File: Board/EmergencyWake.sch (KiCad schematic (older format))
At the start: 128 parts, among them J1 USB_C_Receptacle_USB2.0, J2 Micro_SD_Card_Det, J3 Conn_01x03, J4 Conn_01x02, J5 Conn_01x03, J6 Conn_01x04, J7 Conn_01x02, J8 Conn_01x04, J9 Conn_01x04, Q1 AO3400A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

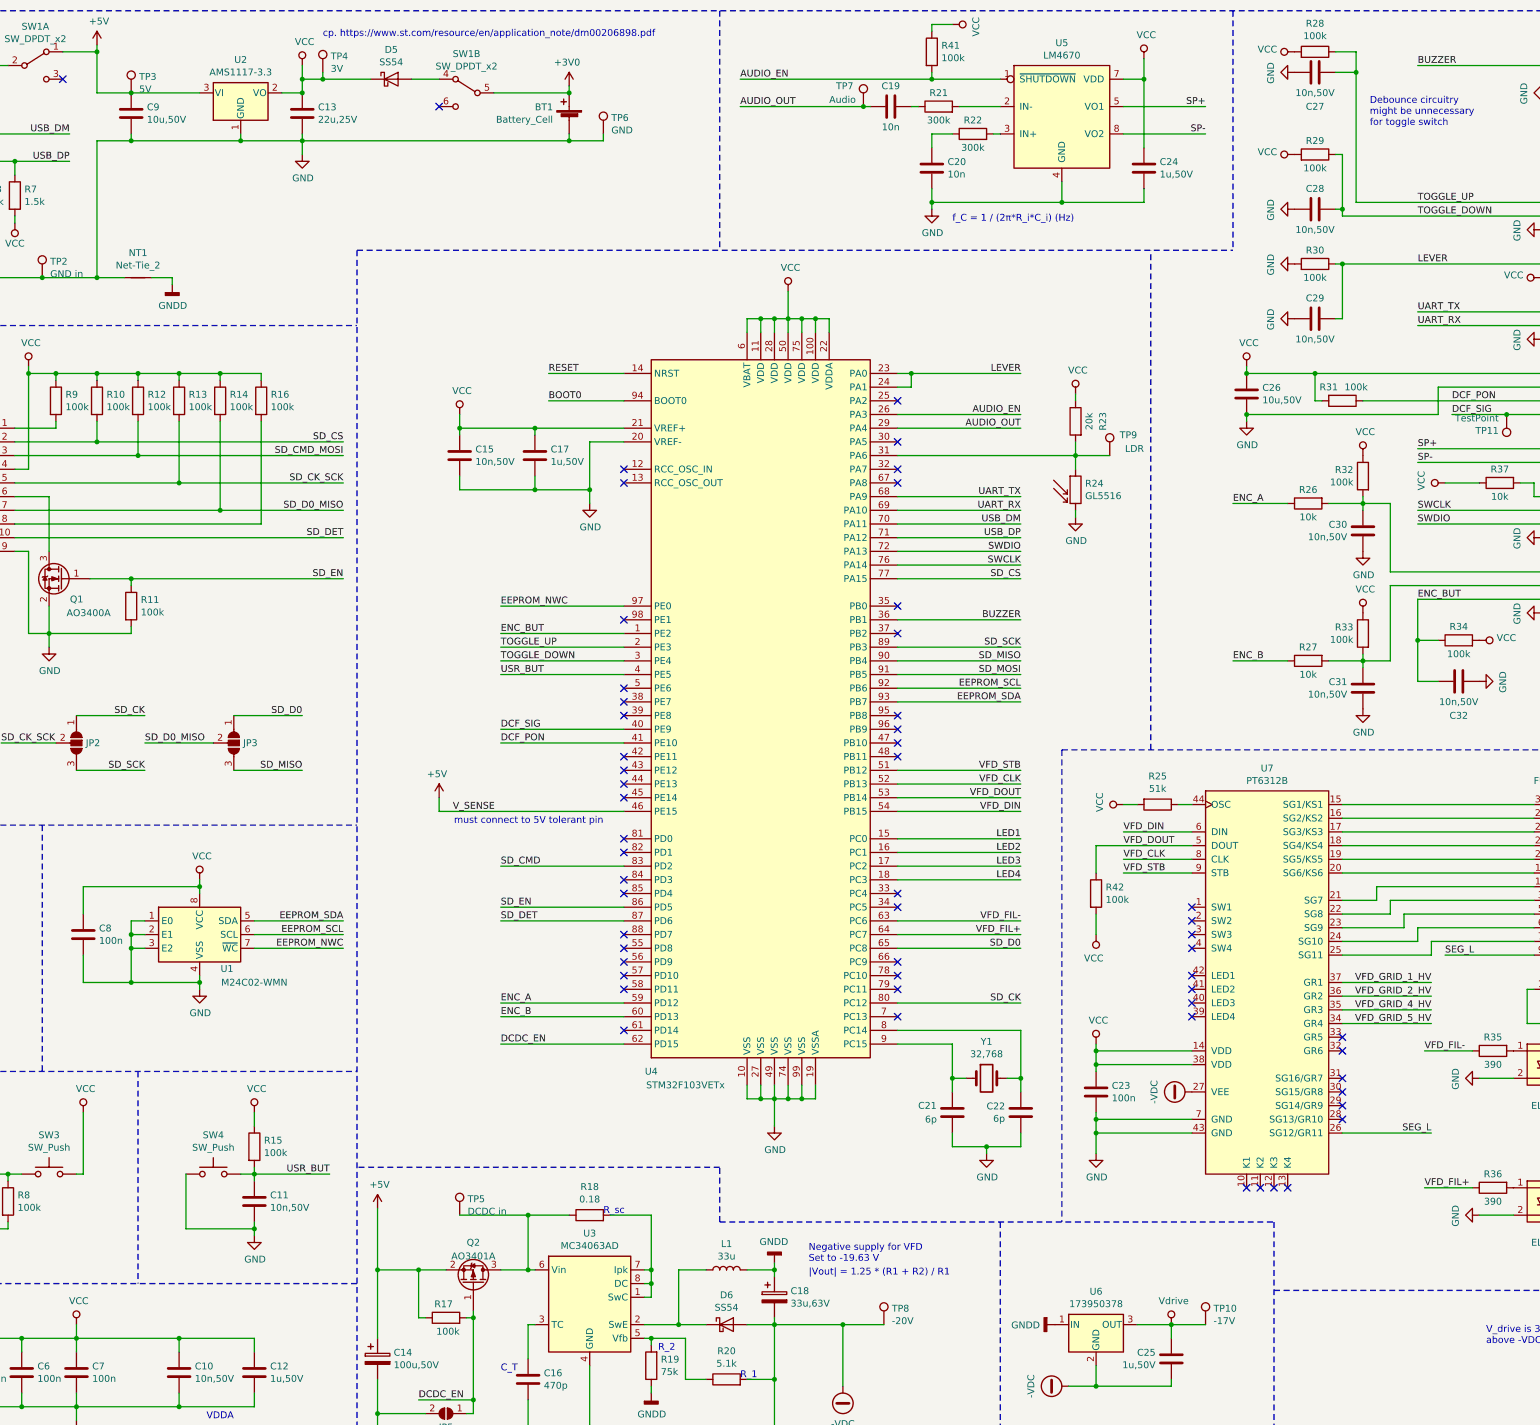
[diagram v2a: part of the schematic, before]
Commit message: [Board] Cleaned up silkscreen
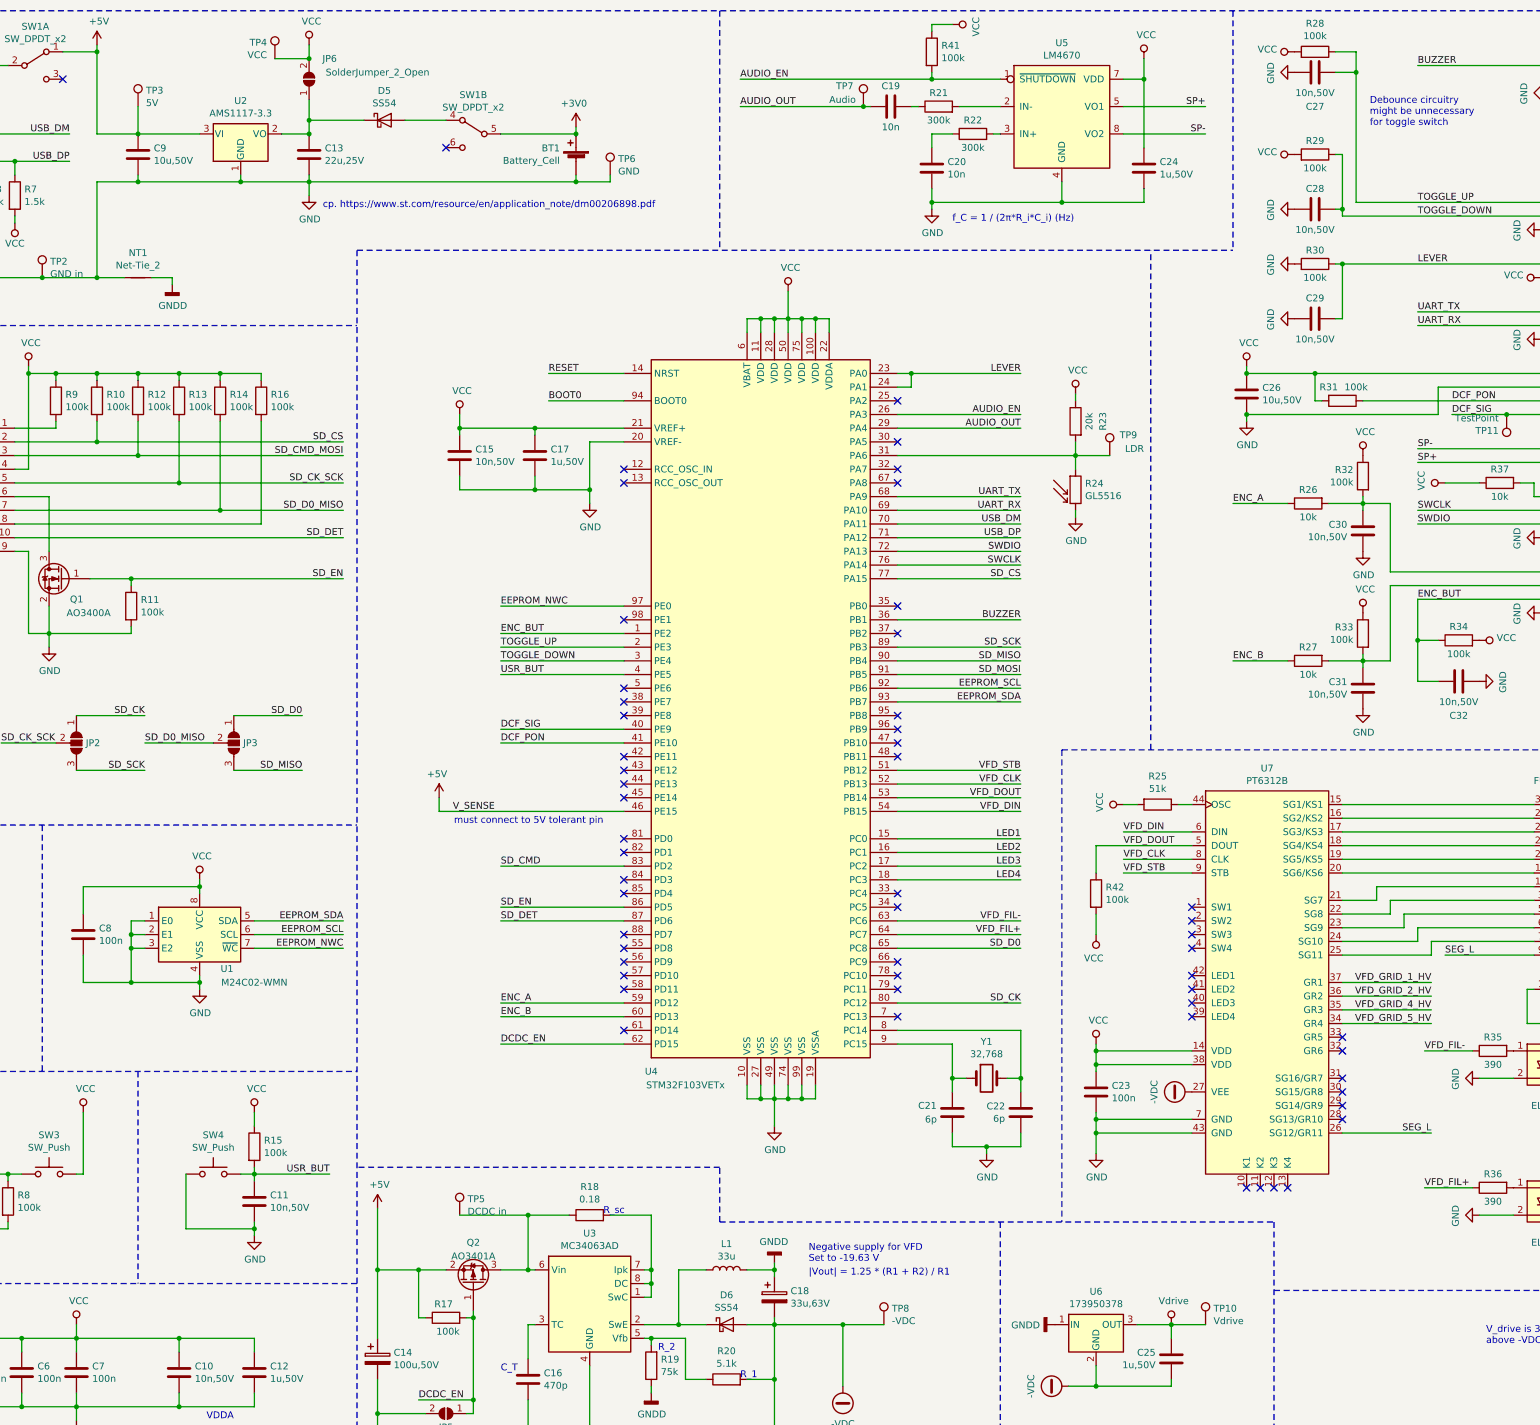
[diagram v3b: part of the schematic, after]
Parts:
- added JP6: SolderJumper_2_Open, Jumper:SolderJumper-2_P1.3mm_Open_TrianglePad1.0x1.5mm, symbol Jumper:SolderJumper_2_Open
- TP10: value -17V -> Vdrive
- TP4: value 3V -> VCC
- TP8: value -20V -> -VDC
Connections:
- net SP+: now also J7.2 (Pin_2); no longer J7.1 (Pin_1)
- net SP-: now also J7.1 (Pin_1); no longer J7.2 (Pin_2)
- net VCC: now also JP6.2 (B); no longer C13.1, D5.1 (K), U2.2 (VO)
- new net: C13.1, D5.1 (K), JP6.1 (A), U2.2 (VO)
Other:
- moved on the sheet: BT1, C13, C9, D5, SW1B, TP3, TP4, TP6, U2
